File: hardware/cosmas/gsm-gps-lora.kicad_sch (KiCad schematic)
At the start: 4 parts, among them U5 SIM800L-CORE

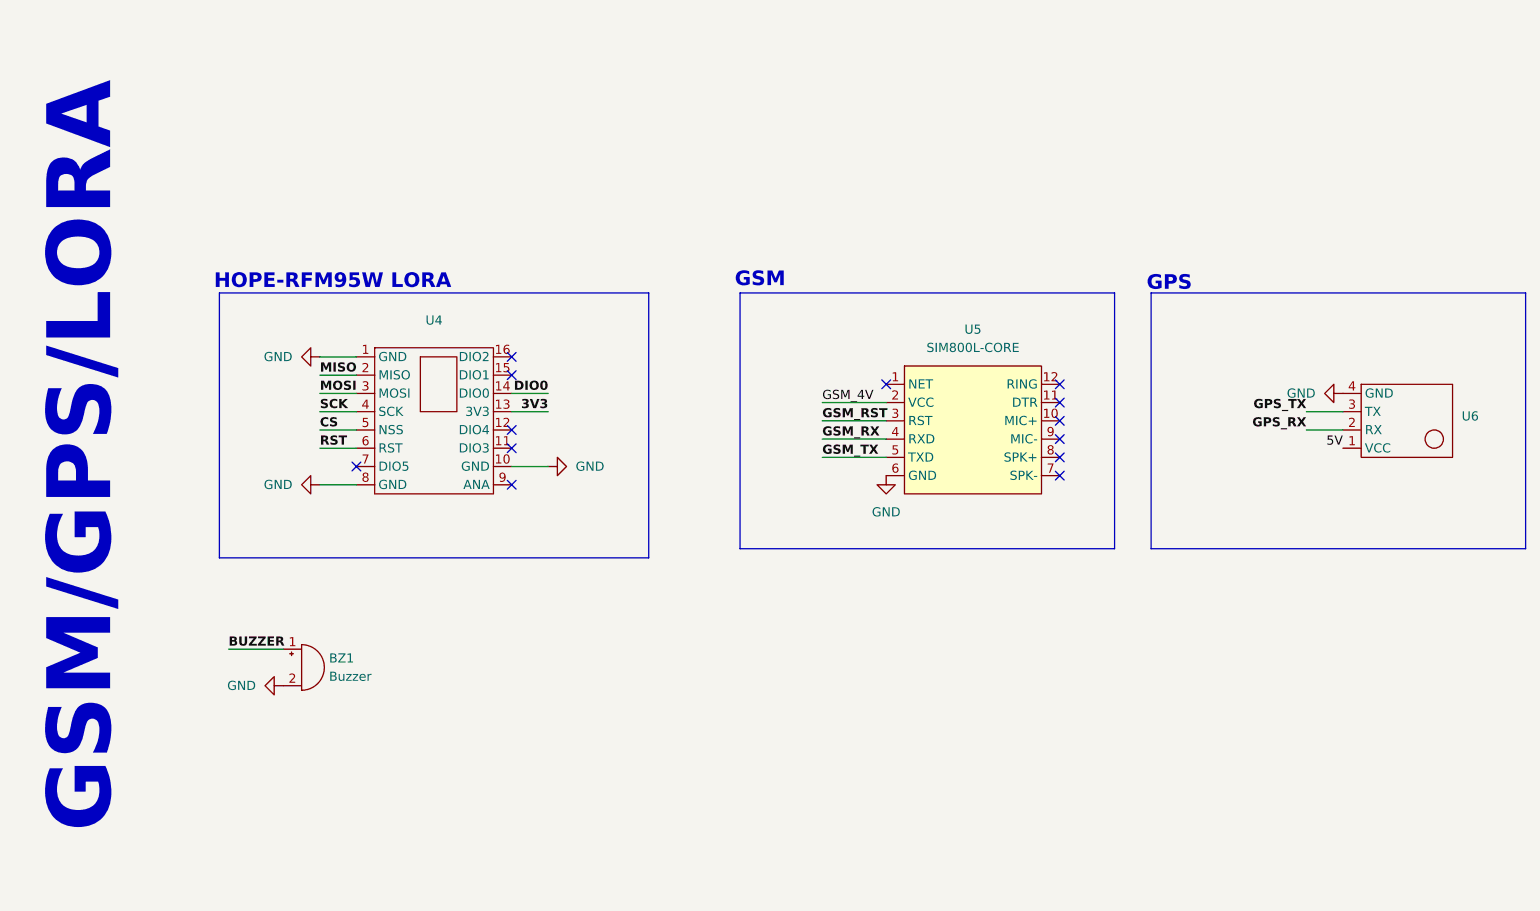
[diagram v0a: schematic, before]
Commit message: updates net labels
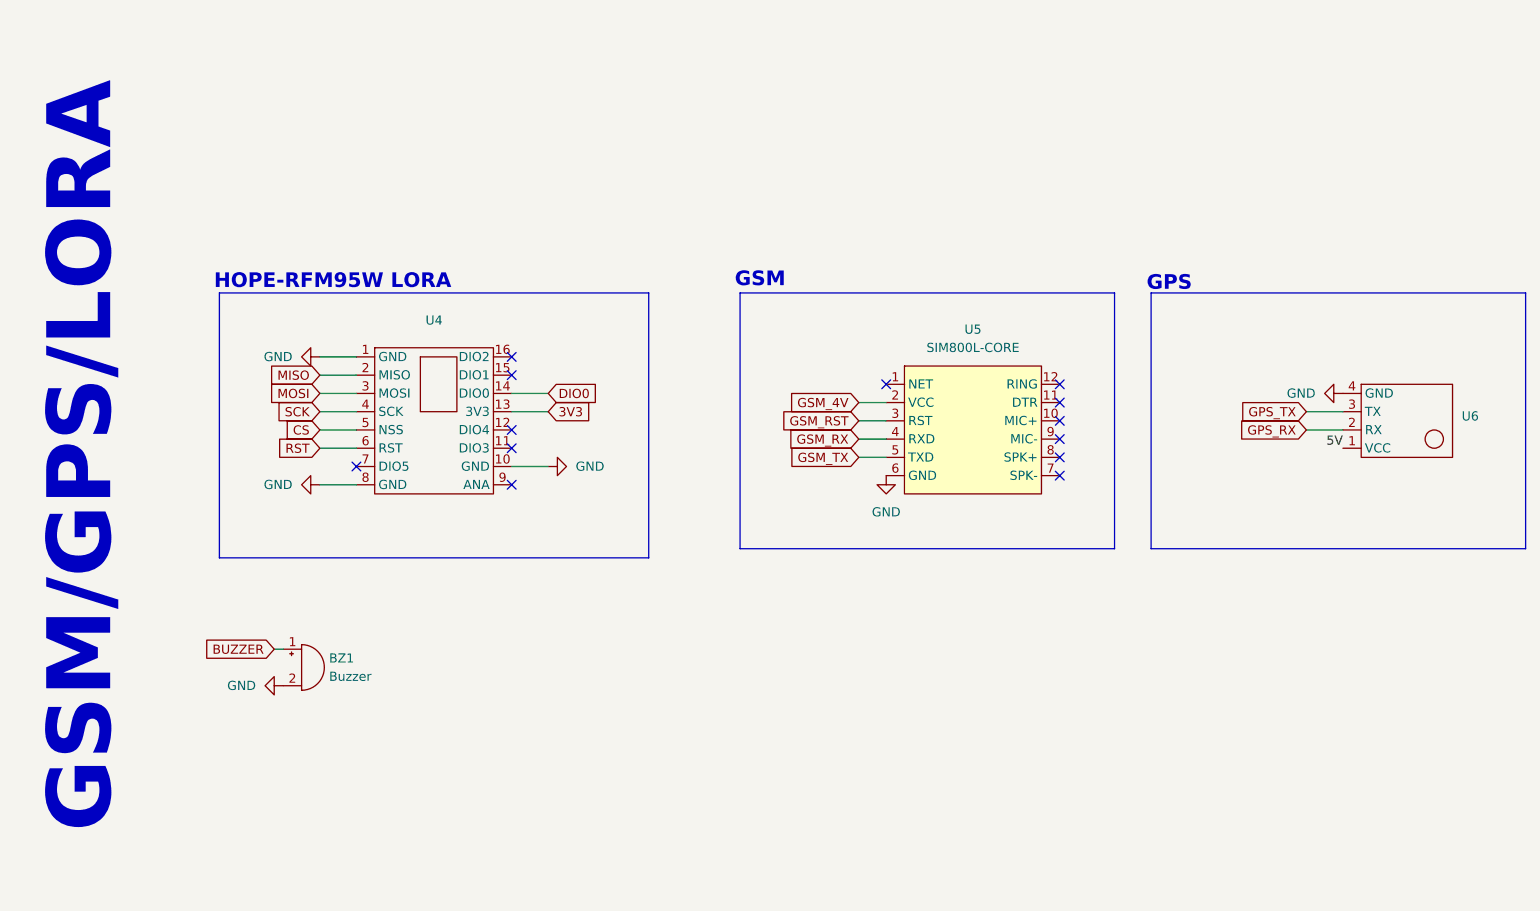
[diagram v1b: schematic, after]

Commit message: adds OBC PCB
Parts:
- added C1: C_Small, Capacitor_THT:CP_Radial_D4.0mm_P2.00mm, symbol Device:C_Small
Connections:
- net GND: now also C1.2; no longer U4.10 (GND), U4.8 (GND)
- net GSM_4V: now also C1.1
- no-connect marks 13 -> 15
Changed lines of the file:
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@@
+	)
+	(no_connect
+		(at 102.87 101.6)
+	)
+	(no_connect
+		(at 81.28 104.14)
 	)
 	(no_connect
@@
 	(wire
 		(pts
-			(xy 102.87 101.6) (xy 107.95 101.6)
-		)
-		(stroke
-			(width 0)
-			(type default)
-		)
-	)
-	(wire
-		(pts
 			(xy 151.13 97.79) (xy 154.94 97.79)
 		)
@@
 	(wire
 		(pts
-			(xy 76.2 104.14) (xy 81.28 104.14)
-		)
-		(stroke
-			(width 0)
-			(type default)
-		)
-	)
-	(wire
-		(pts
 			(xy 76.2 96.52) (xy 81.28 96.52)
 		)
@@
 		(pts
 			(xy 102.87 91.44) (xy 107.95 91.44)
+		)
+		(stroke
+			(width 0)
+			(type default)
+		)
+	)
+	(wire
+		(pts
+			(xy 213.36 99.06) (xy 218.44 99.06)
 		)
 		(stroke
@@
 		)
 	)
-	(label "5V"
-		(at 218.44 99.06 180)
-		(fields_autoplaced yes)
-		(effects
-			(font
-				(size 1.27 1.27)
-			)
-			(justify right bottom)
-		)
-	)
 	(global_label "GSM_TX"
 		(shape input)
@@
 		)
 	)
+	(global_label "GSM_4V"
+		(shape input)
+		(at 143.51 81.28 180)
+		(fields_autoplaced yes)
+		(effects
+			(font
+				(size 1.27 1.27)
+			)
+			(justify right)
+		)
+		(property "Intersheetrefs" "${INTERSHEET_REFS}"
+			(at 133.3282 81.28 0)
+			(effects
+				(font
+					(size 1.27 1.27)
+				)
+				(justify right)
+				(hide yes)
+			)
+		)
+	)
 	(global_label "SCK"
 		(shape input)
@@
 		(property "Intersheetrefs" "${INTERSHEET_REFS}"
 			(at 69.7677 99.06 0)
+			(effects
+				(font
+					(size 1.27 1.27)
+				)
+				(justify right)
+				(hide yes)
+			)
+		)
+	)
+	(global_label "5V"
+		(shape input)
+		(at 213.36 99.06 180)
+		(fields_autoplaced yes)
+		(effects
+			(font
+				(size 1.27 1.27)
+			)
+			(justify right)
+		)
+		(property "Intersheetrefs" "${INTERSHEET_REFS}"
+			(at 208.0767 99.06 0)
 			(effects
 				(font
@@
 	)
 	(symbol
-		(lib_id "power:GND")
-		(at 107.95 101.6 90)
-		(unit 1)
-		(exclude_from_sim no)
-		(in_bom yes)
-		(on_board yes)
-		(dnp no)
-		(fields_autoplaced yes)
-		(property "Reference" "#PWR08"
-			(at 114.3 101.6 0)
-			(effects
-				(font
-					(size 1.27 1.27)
-				)
-				(hide yes)
-			)
-		)
-		(property "Value" "GND"
-			(at 111.76 101.5999 90)
-			(effects
-				(font
-					(size 1.27 1.27)
-				)
-				(justify right)
-			)
-		)
-		(property "Footprint" ""
-			(at 107.95 101.6 0)
-			(effects
-				(font
-					(size 1.27 1.27)
-				)
-				(hide yes)
-			)
-		)
-		(property "Datasheet" ""
-			(at 107.95 101.6 0)
-			(effects
-				(font
-					(size 1.27 1.27)
-				)
-				(hide yes)
-			)
-		)
-		(property "Description" "Power symbol creates a global label with name \"GND\" , ground"
-			(at 107.95 101.6 0)
-			(effects
-				(font
-					(size 1.27 1.27)
-				)
-				(hide yes)
-			)
-		)
-		(pin "1"
-		)
-		(instances
-			(project ""
-				(path "/bb87b3c4-a185-4d09-b637-e12eb905a163/6a26fb06-24b3-4562-a35b-864dc5cf9817"
-					(reference "#PWR08")
-					(unit 1)
-				)
-			)
-		)
-	)
-	(symbol
 		(lib_id "Device:Buzzer")
 		(at 73.66 129.54 0)
@@
 	(symbol
 		(lib_id "power:GND")
-		(at 76.2 104.14 270)
-		(unit 1)
-		(exclude_from_sim no)
-		(in_bom yes)
-		(on_board yes)
-		(dnp no)
-		(fields_autoplaced yes)
-		(property "Reference" "#PWR010"
-			(at 69.85 104.14 0)
-			(effects
-				(font
-					(size 1.27 1.27)
-				)
-				(hide yes)
-			)
-		)
-		(property "Value" "GND"
-			(at 72.39 104.1399 90)
-			(effects
-				(font
-					(size 1.27 1.27)
-				)
-				(justify right)
-			)
-		)
-		(property "Footprint" ""
-			(at 76.2 104.14 0)
-			(effects
-				(font
-					(size 1.27 1.27)
-				)
-				(hide yes)
-			)
-		)
-		(property "Datasheet" ""
-			(at 76.2 104.14 0)
-			(effects
-				(font
-					(size 1.27 1.27)
-				)
-				(hide yes)
-			)
-		)
-		(property "Description" "Power symbol creates a global label with name \"GND\" , ground"
-			(at 76.2 104.14 0)
-			(effects
-				(font
-					(size 1.27 1.27)
-				)
-				(hide yes)
-			)
-		)
-		(pin "1"
-		)
-		(instances
-			(project "cosmas"
-				(path "/bb87b3c4-a185-4d09-b637-e12eb905a163/6a26fb06-24b3-4562-a35b-864dc5cf9817"
-					(reference "#PWR010")
-					(unit 1)
-				)
-			)
-		)
-	)
-	(symbol
-		(lib_id "power:GND")
 		(at 71.12 132.08 270)
 		(unit 1)
@@
 					(unit 1)
 				)
+			)
+		)
+	)
+	(symbol
+		(lib_id "power:GND")
+		(at 143.51 86.36 0)
+		(unit 1)
+		(exclude_from_sim no)
+		(in_bom yes)
+		(on_board yes)
+		(dnp no)
+		(property "Reference" "#PWR017"
+			(at 143.51 92.71 0)
+			(effects
+				(font
+					(size 1.27 1.27)
+				)
+				(hide yes)
+			)
+		)
+		(property "Value" "GND"
+			(at 143.51 90.17 0)
+			(effects
+				(font
+					(size 1.27 1.27)
+				)
+			)
+		)
+		(property "Footprint" ""
+			(at 143.51 86.36 0)
+			(effects
+				(font
+					(size 1.27 1.27)
+				)
+				(hide yes)
+			)
+		)
+		(property "Datasheet" ""
+			(at 143.51 86.36 0)
+			(effects
+				(font
+					(size 1.27 1.27)
+				)
+				(hide yes)
+			)
+		)
+		(property "Description" "Power symbol creates a global label with name \"GND\" , ground"
+			(at 143.51 86.36 0)
+			(effects
+				(font
+					(size 1.27 1.27)
+				)
+				(hide yes)
+			)
+		)
+		(pin "1"
+		)
+		(instances
+			(project "cosmas"
+				(path "/bb87b3c4-a185-4d09-b637-e12eb905a163/6a26fb06-24b3-4562-a35b-864dc5cf9817"
+					(reference "#PWR017")
+					(unit 1)
+				)
+			)
+		)
+	)
+	(symbol
+		(lib_id "Device:C_Small")
+		(at 143.51 83.82 0)
+		(unit 1)
+		(exclude_from_sim no)
+		(in_bom yes)
+		(on_board yes)
+		(dnp no)
+		(fields_autoplaced yes)
+		(property "Reference" "C1"
+			(at 146.05 82.5562 0)
+			(effects
+				(font
+					(size 1.27 1.27)
+				)
+				(justify left)
+			)
+		)
+		(property "Value" "C_Small"
+			(at 146.05 85.0962 0)
+			(effects
+				(font
+					(size 1.27 1.27)
+				)
+				(justify left)
+			)
+		)
+		(property "Footprint" "Capacitor_THT:CP_Radial_D4.0mm_P2.00mm"
+			(at 143.51 83.82 0)
+			(effects
+				(font
+					(size 1.27 1.27)
+				)
+				(hide yes)
+			)
+		)
+		(property "Datasheet" "~"
+			(at 143.51 83.82 0)
+			(effects
+				(font
+					(size 1.27 1.27)
+				)
+				(hide yes)
+			)
+		)
+		(property "Description" "Unpolarized capacitor, small symbol"
+			(at 143.51 83.82 0)
+			(effects
+				(font
+					(size 1.27 1.27)
+				)
+				(hide yes)
+			)
+		)
+		(pin "2"
+		)
+		(pin "1"
+		)
+		(instances
+			(project ""
+				(path "/bb87b3c4-a185-4d09-b637-e12eb905a163/6a26fb06-24b3-4562-a35b-864dc5cf9817"
+					(reference "C1")
+					(unit 1)
+				)
